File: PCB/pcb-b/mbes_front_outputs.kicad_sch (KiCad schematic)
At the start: 58 parts, among them Q1 BC817, Q10 BC817, Q11 TPCA8120,L1Q, Q14 BC817, Q15 BC817, Q19 BC817, Q2 BC817, Q20 BC817, Q21 BC817, Q4 TPCA8120,L1Q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

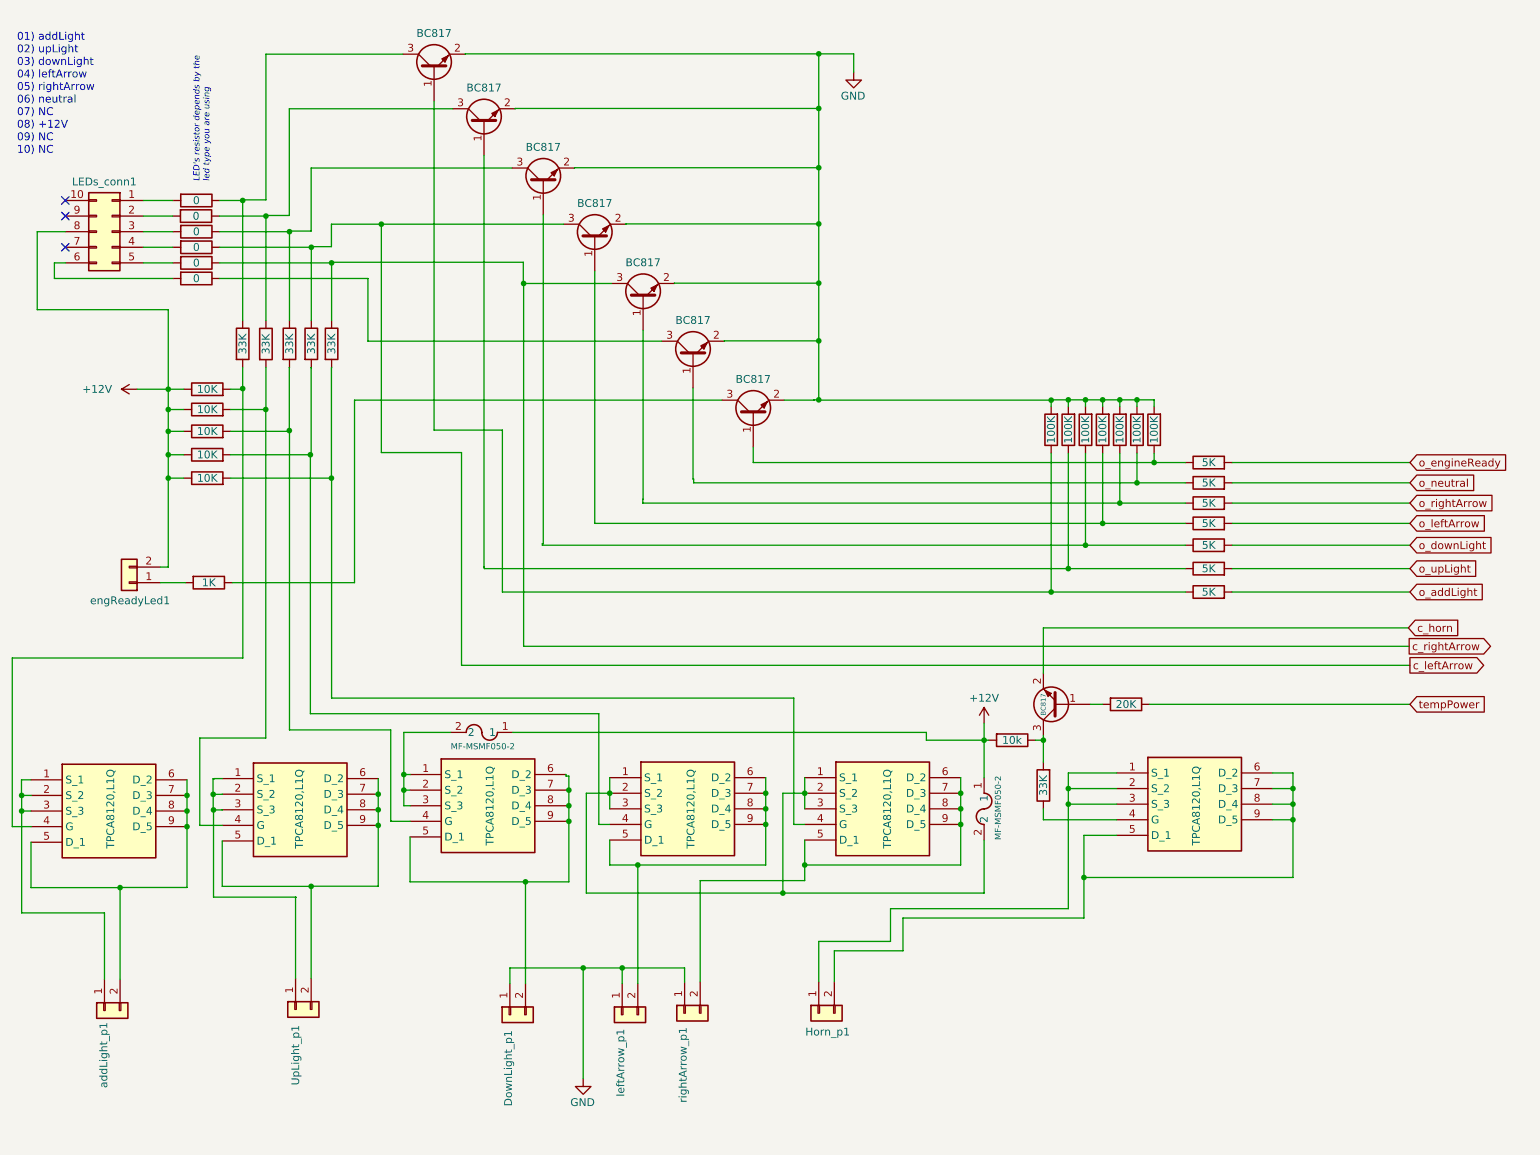
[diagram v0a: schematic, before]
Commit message: PCB(b) size reduction and unuseful resistors removed
Originally, I placed resistors between the MOSFET's gate and the NPN collector to reduce the possible VGS voltage difference.
But, reading the TCPA8120's datasheet I have seen it accepts VGS max -20!! But in motorbike battey I never see 20 volts. So,
I removed the resistors. Now, when the NPN is conducing then the VGS will be about -12 volts, it is also better to avoid the
MOSFETs work in linear mode.

Thank to this component removing, also the PCB size has been reduced (85.6mm x 40.0mm). But, in order to get the size reduction
the add-light connector has been splitted in two single wite connectors. It is not beautiful to see, bet the PCB size is a too
big problem, and multilayer solution is a too expensive one!
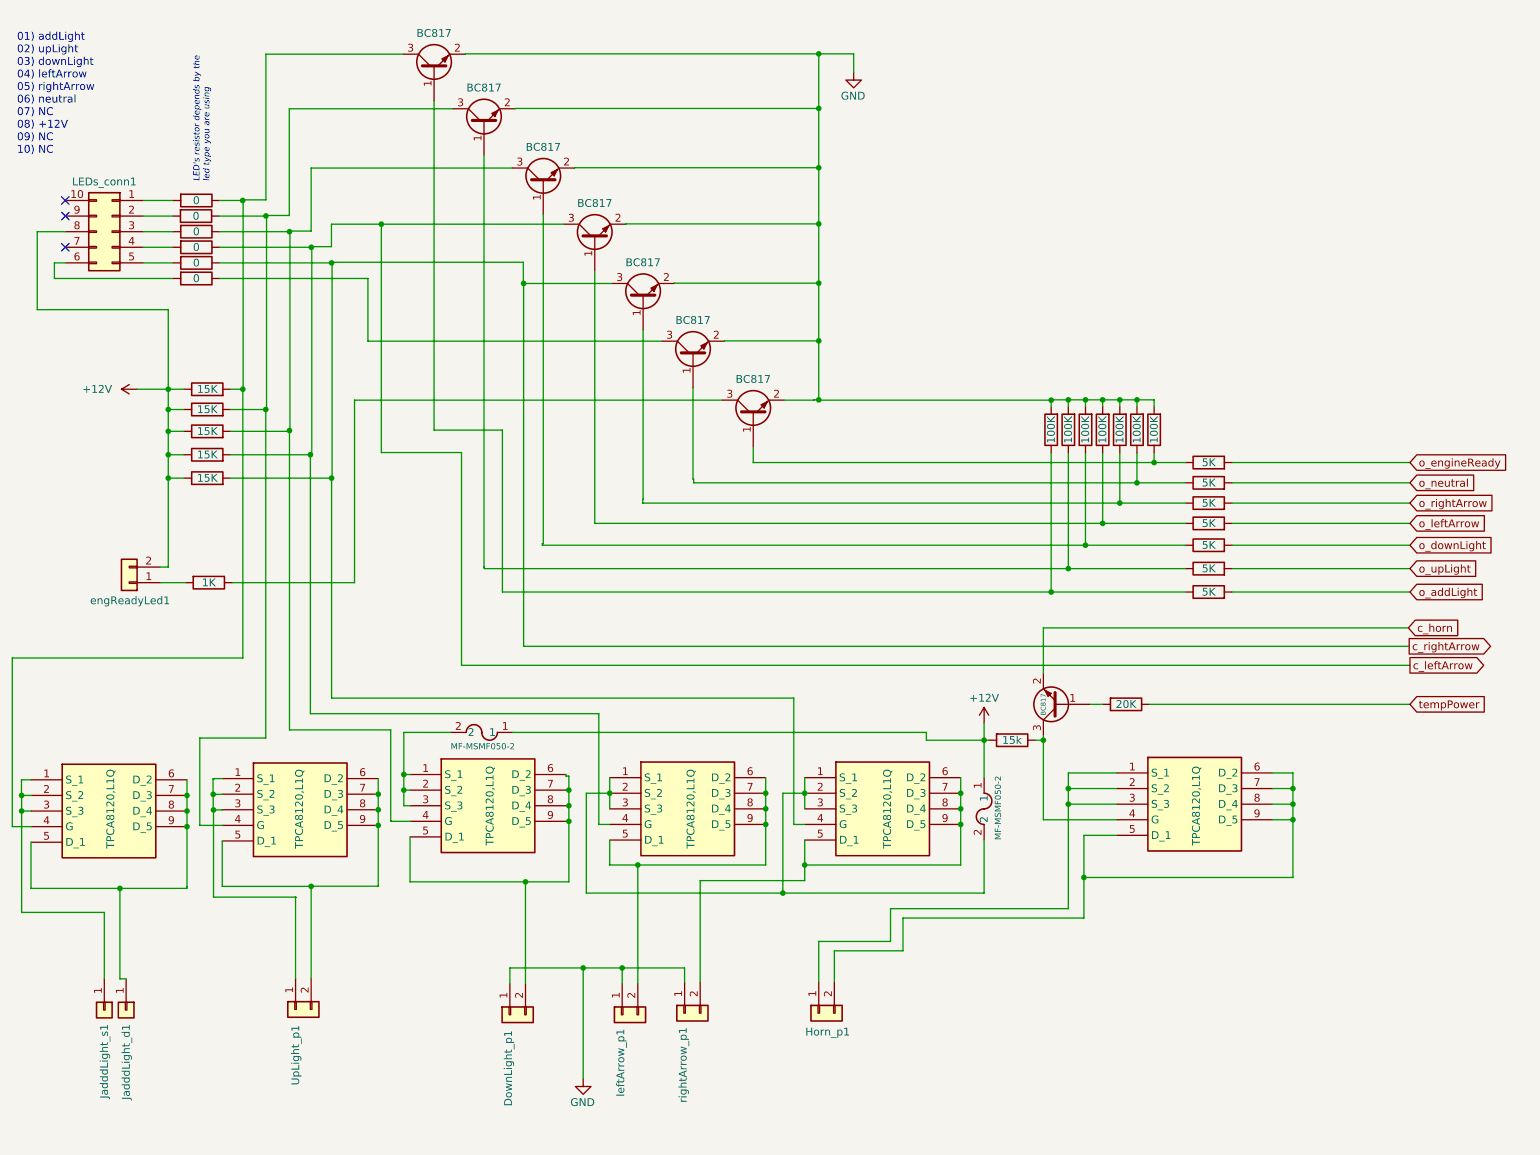
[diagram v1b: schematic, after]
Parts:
- removed RA10, RA11, RA12, RA13, RA14, RA7: 33K, Resistor_SMD:R_1206_3216Metric, symbol Device:R
- removed addLight_p1: Conn_01x02, Connector_Wire:SolderWire-0.75sqmm_1x02_P4.8mm_D1.25mm_OD2.3mm, symbol Connector_Generic:Conn_01x02
- added JadddLight_d1, JadddLight_s1: Conn_01x01, Connector_Wire:SolderWire-1sqmm_1x01_D1.4mm_OD2.7mm, symbol Connector_Generic:Conn_01x01
- RA24, RA25, RA26, RA27, RA28: value 10K -> 15K
- RA42: value 10k -> 15k
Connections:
- net c_leftArrow: now also Q6.4 (G), RA27.2
- net c_rightArrow: now also Q7.4 (G), RA28.2
- net at Q1.3 (C), RA1.1: now also Q11.4 (G), RA24.2
- net at Q5.4 (G), RA26.2: now also Q14.3 (C), RA3.1
- net at Q11.1 (S_1), Q11.2 (S_2), Q11.3 (S_3): now also JadddLight_s1.1 (Pin_1)
- net at Q11.5 (D_1), Q11.6 (D_2), Q11.7 (D_3)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: now also JadddLight_d1.1 (Pin_1)
- net at Q4.4 (G), RA25.2: now also Q2.3 (C), RA2.1
- net at Q8.4 (G): now also Q10.3 (C), RA42.1

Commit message: Floating FET's source pin fixed
The pin was in floating state when the associated external fuse is burnt
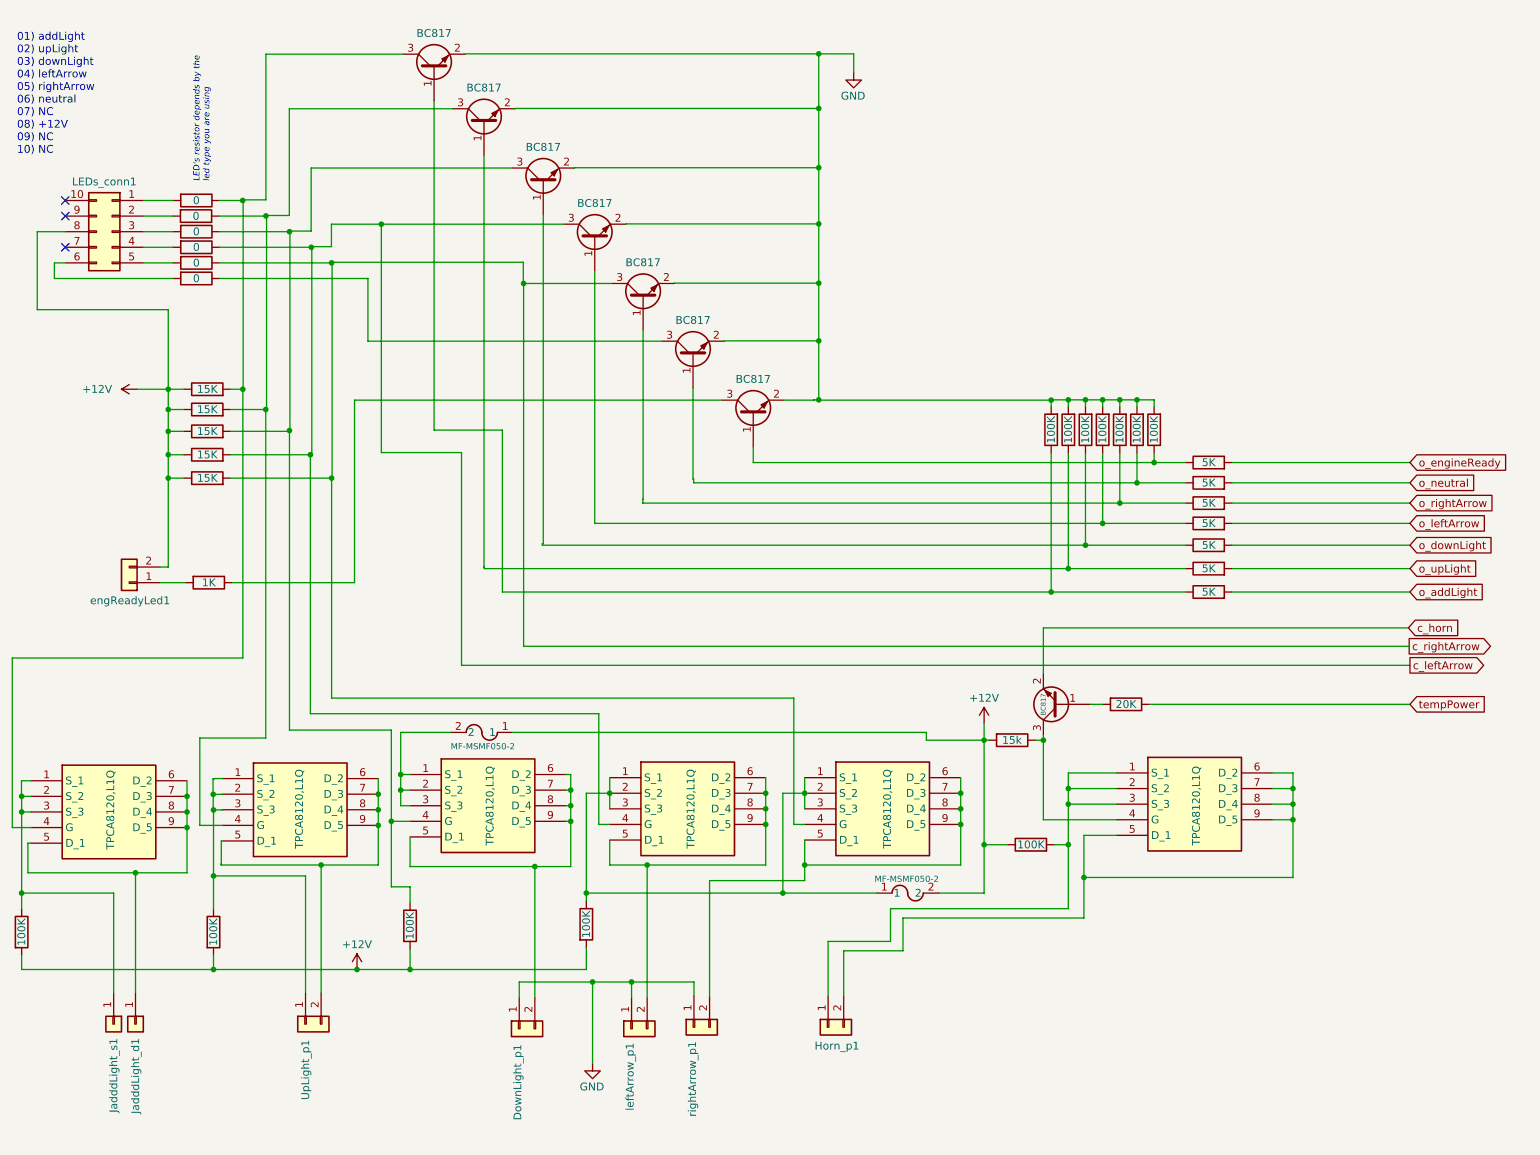
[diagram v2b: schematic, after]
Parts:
- added RA10, RA11, RA12, RA13, RA7: 100K, Resistor_SMD:R_1206_3216Metric, symbol Device:R
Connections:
- net +12V: now also F2.2, RA10.2, RA11.2, RA12.2, RA13.1, RA7.2; no longer F2.1
- net at Q14.3 (C), Q5.4 (G), RA26.2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: now also RA11.1
- net at Q6.1 (S_1), Q6.2 (S_2), Q6.3 (S_3)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: now also F2.1, RA12.1; no longer F2.2
- net at JadddLight_s1.1 (Pin_1), Q11.1 (S_1), Q11.2 (S_2)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: now also RA7.1
- net at Horn_p1.1 (Pin_1), Q8.1 (S_1), Q8.2 (S_2)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: now also RA13.2
- net at Q4.1 (S_1), Q4.2 (S_2), Q4.3 (S_3)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: now also RA10.1
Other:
- moved on the sheet: DownLight_p1, Horn_p1, JadddLight_d1, JadddLight_s1, UpLight_p1, leftArrow_p1, rightArrow_p1

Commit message: ...
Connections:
- net at Q14.3 (C), Q5.4 (G), RA26.2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: no longer RA11.1
- net at F1.2, Q5.1 (S_1), Q5.2 (S_2)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: now also RA11.1
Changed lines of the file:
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@@
 	)
 	(junction
+		(at 78.74 143.002)
+		(diameter 0)
+		(color 0 0 0 0)
+	)
+	(junction
 		(at 75.0824 143.6624)
 		(diameter 0)
@@
 	)
 	(junction
-		(at 77.216 145.542)
-		(diameter 0)
-		(color 0 0 0 0)
-	)
-	(junction
 		(at 98.7552 57.9628)
 		(diameter 0)
@@
 	(wire
 		(pts
-			(xy 77.216 156.21) (xy 80.264 156.21)
-		)
-		(stroke
-			(width 0)
-			(type default)
-		)
-	)
-	(wire
-		(pts
 			(xy 32.004 157.226) (xy 32.004 173.482)
 		)
@@
 	(wire
 		(pts
+			(xy 78.74 156.21) (xy 80.264 156.21)
+		)
+		(stroke
+			(width 0)
+			(type default)
+		)
+	)
+	(wire
+		(pts
 			(xy 98.7552 117.0432) (xy 242.951 117.0432)
 		)
@@
 	(wire
 		(pts
-			(xy 77.216 145.542) (xy 77.216 156.21)
-		)
-		(stroke
-			(width 0)
-			(type default)
-		)
-	)
-	(wire
-		(pts
 			(xy 22.352 57.15) (xy 41.656 57.15)
 		)
@@
 		)
 		(stroke
+			(width 0)
+			(type default)
+		)
+	)
+	(wire
+		(pts
+			(xy 78.74 143.002) (xy 78.74 156.21)
+		)
+		(stroke
